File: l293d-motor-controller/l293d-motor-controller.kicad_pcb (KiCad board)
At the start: 2 copper layers, 49.6 x 66 mm, 19 parts, among them M1 Motor_DC, M2 Motor_DC, U1 LM7805, U2 L293D, U3 74HC04

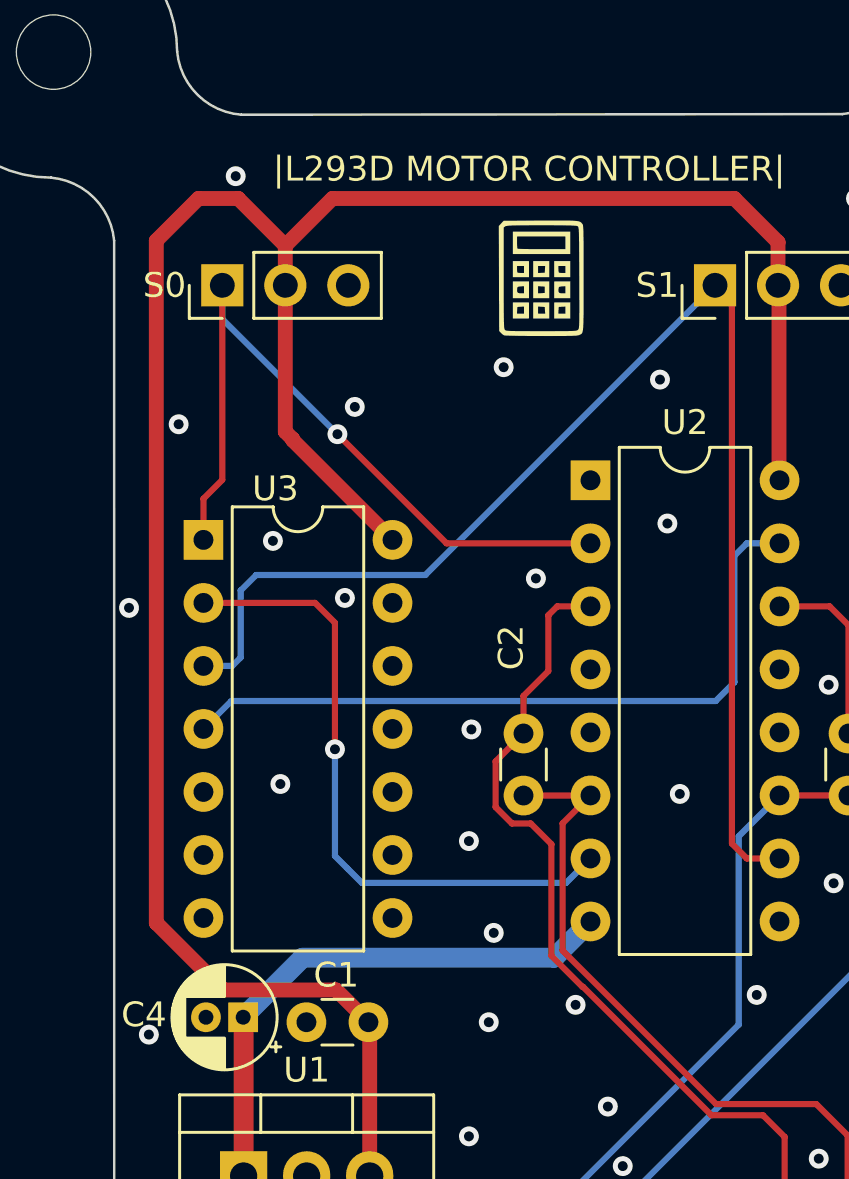
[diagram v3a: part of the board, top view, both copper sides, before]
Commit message: project 3 / l293d motor driver / 74hc04 changed to cd4069
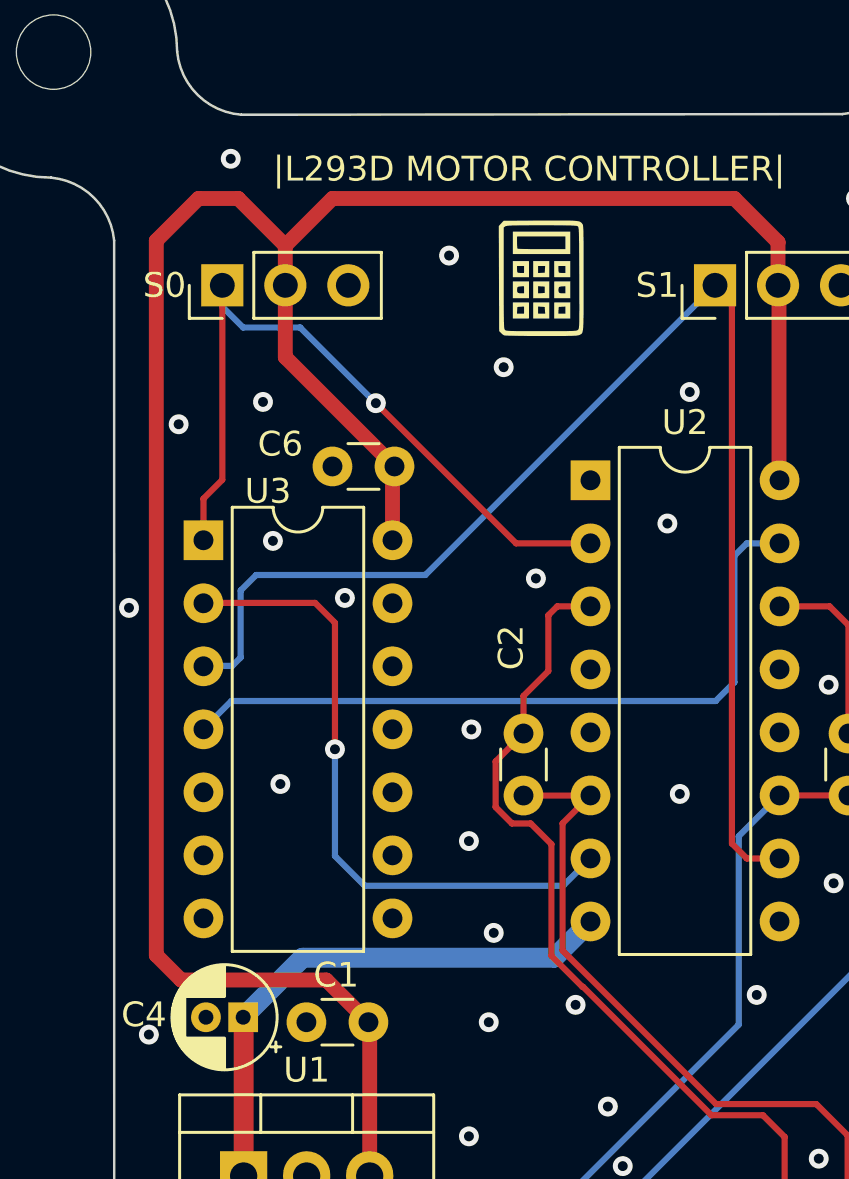
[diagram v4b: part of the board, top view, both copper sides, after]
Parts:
- added C6: 100n, Capacitor_THT:C_Disc_D3.0mm_W1.6mm_P2.50mm, F.Cu at (116.6, 110.7)
- U3: value 74HC04 -> 4069
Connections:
- U3 pad 11: unconnected-(U3-Q5-Pad11) -> GND
- U3 pad 13: unconnected-(U3-Q7-Pad13) -> GND
- U3 pad 5: unconnected-(U3-Q2-Pad5) -> GND
- U3 pad 9: unconnected-(U3-~{MR}-Pad9) -> GND
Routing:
- net +5V: track 96.0 -> 96.7 mm
- net GND: vias 35 -> 36

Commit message: project 3 / l293d motor controller / improved tracs
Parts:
- moved M1 10.3 mm to (121.8, 144.3)
- moved M2 8.38 mm to (132.2, 144.4)
- moved BT1 1.10 mm to (117.3, 144.3)
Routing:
- net Net-(M1--): track 30.7 -> 24.2 mm
- net Net-(M1-+): track 36.9 -> 31.0 mm
- net Net-(M2--): track 34.8 -> 31.6 mm
- net Net-(M2-+): track 26.7 -> 24.4 mm
- net +9V: track 36.1 -> 35.0 mm
- net GND: vias 36 -> 34

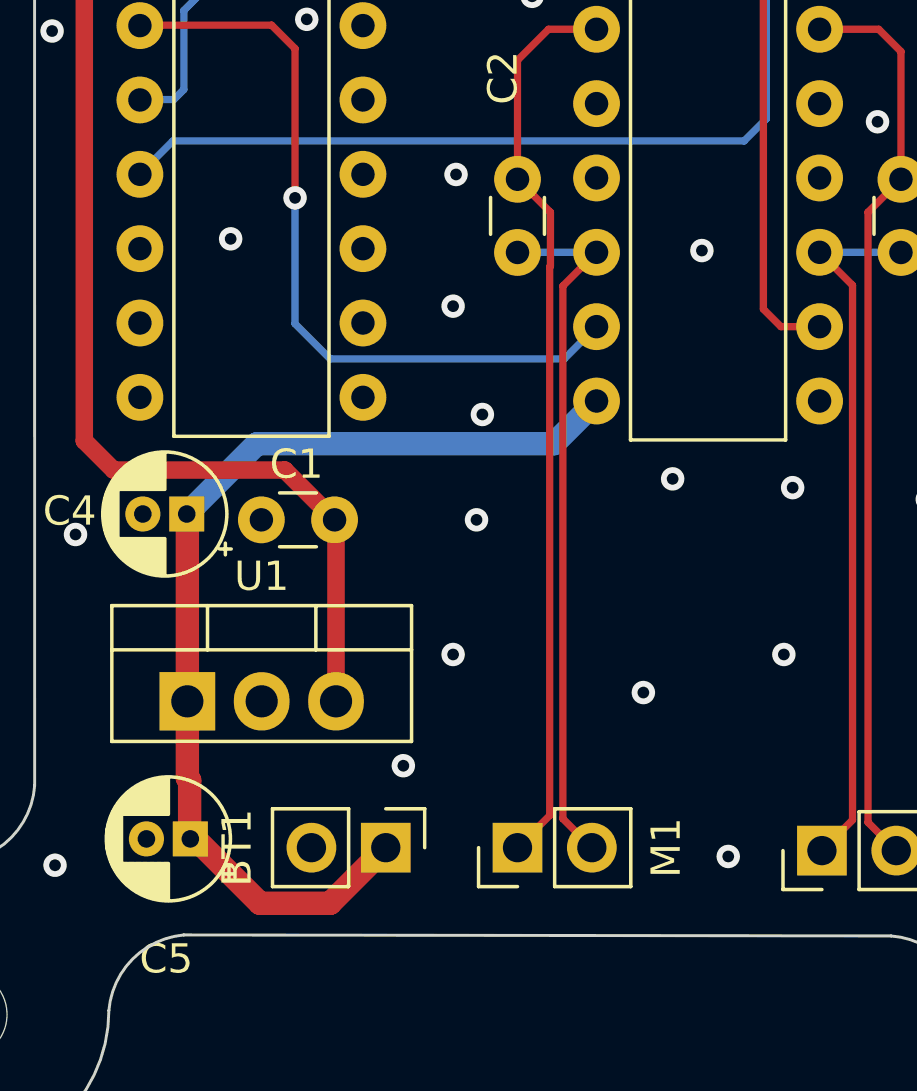
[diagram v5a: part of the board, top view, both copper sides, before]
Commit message: project 3 / l293d motor driver / VCC track changed
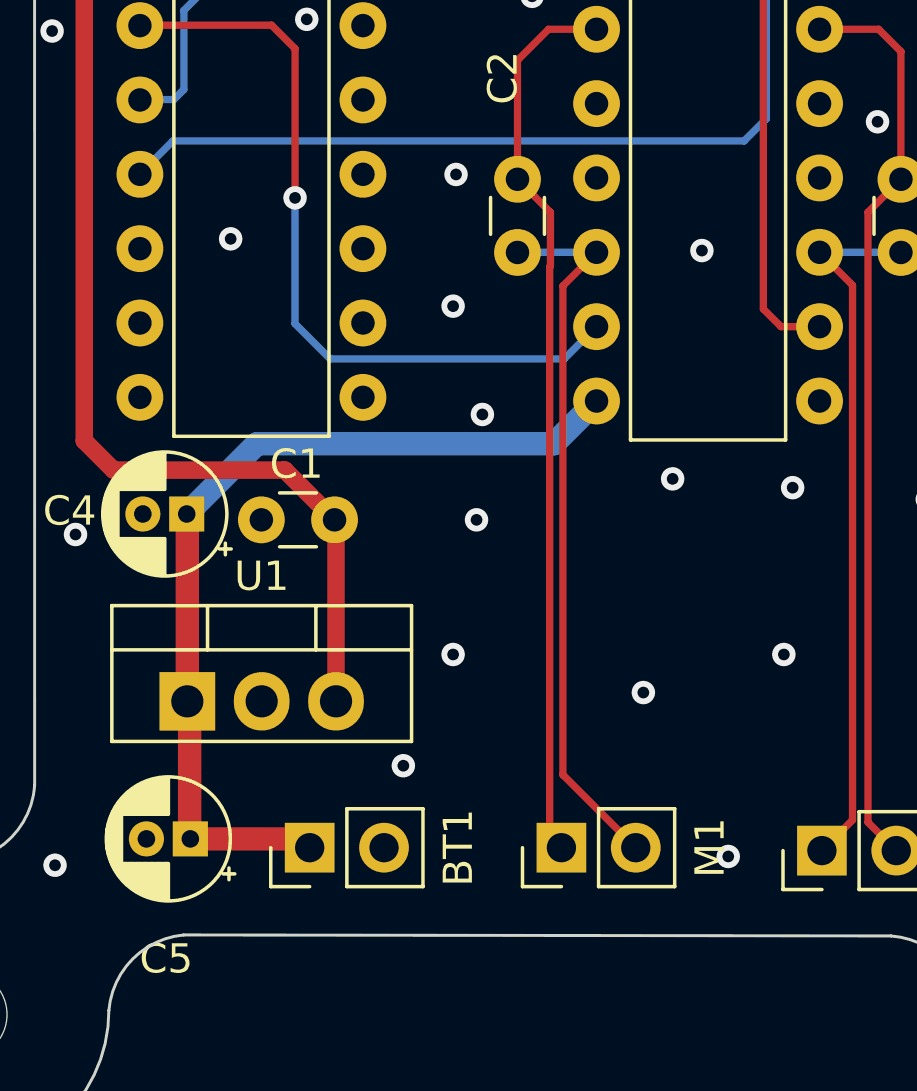
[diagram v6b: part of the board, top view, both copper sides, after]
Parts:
- moved BT1 2.60 mm to (114.7, 144.3), turned to 90 degrees
- moved M1 1.50 mm to (123.3, 144.3)
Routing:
- net +9V: track 35.0 -> 30.8 mm
- net Net-(M1--): track 24.2 -> 24.7 mm
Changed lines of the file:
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@@
   )
   (footprint "Connector_PinHeader_2.54mm:PinHeader_1x02_P2.54mm_Vertical" (layer "F.Cu")
-    (at 117.3 144.3 -90)
+    (at 114.7 144.3 90)
     (descr "Through hole straight pin header, 1x02, 2.54mm pitch, single row")
     (tags "Through hole pin header THT 1x02 2.54mm single row")
@@
     (fp_line (start 1.27 3.81) (end -1.27 3.81)
       (stroke (width 0.1) (type solid)) (layer "F.Fab"))
-    (pad "1" thru_hole rect (at 0 0 270) (size 1.7 1.7) (drill 1) (layers "*.Cu" "*.Mask")
+    (pad "1" thru_hole rect (at 0 0 90) (size 1.7 1.7) (drill 1) (layers "*.Cu" "*.Mask")
       (net 1 "+9V") (pinfunction "+") (pintype "passive"))
-    (pad "2" thru_hole oval (at 0 2.54 270) (size 1.7 1.7) (drill 1) (layers "*.Cu" "*.Mask")
+    (pad "2" thru_hole oval (at 0 2.54 90) (size 1.7 1.7) (drill 1) (layers "*.Cu" "*.Mask")
       (net 2 "GND") (pinfunction "-") (pintype "passive"))
     (model "${KICAD6_3DMODEL_DIR}/Connector_PinHeader_2.54mm.3dshapes/PinHeader_1x02_P2.54mm_Vertical.wrl"
@@
   )
   (footprint "Connector_PinHeader_2.54mm:PinHeader_1x02_P2.54mm_Vertical" (layer "F.Cu")
-    (at 121.8 144.3 90)
+    (at 123.3 144.3 90)
     (descr "Through hole straight pin header, 1x02, 2.54mm pitch, single row")
     (tags "Through hole pin header THT 1x02 2.54mm single row")
@@
     (effects (font (size 1 1) (thickness 0.15)) (justify left bottom))
   )
-  (segment (start 110.8 144) (end 113 146.2) (width 0.8) (layer "F.Cu") (net 1))
+  (segment (start 114.4 144) (end 114.7 144.3) (width 0.8) (layer "F.Cu") (net 1))
+  (segment (start 110.6226 144) (end 114.4 144) (width 0.8) (layer "F.Cu") (net 1))
   (segment (start 110.52 132.92) (end 110.5 132.9) (width 0.8) (layer "F.Cu") (net 1))
-  (segment (start 110.6 142) (end 110.52 141.92) (width 0.8) (layer "F.Cu") (net 1))
+  (segment (start 110.6 139.38) (end 110.52 139.3) (width 0.8) (layer "F.Cu") (net 1))
   (segment (start 110.52 139.3) (end 110.52 132.92) (width 0.8) (layer "F.Cu") (net 1))
-  (segment (start 115.4 146.2) (end 117.3 144.3) (width 0.8) (layer "F.Cu") (net 1))
-  (segment (start 113 146.2) (end 115.4 146.2) (width 0.8) (layer "F.Cu") (net 1))
-  (segment (start 110.6226 144) (end 110.8 144) (width 0.8) (layer "F.Cu") (net 1))
-  (segment (start 110.52 141.92) (end 110.52 139.3) (width 0.8) (layer "F.Cu") (net 1))
-  (segment (start 110.6 143.9) (end 110.6 142) (width 0.8) (layer "F.Cu") (net 1))
+  (segment (start 110.6 143.9) (end 110.6 139.38) (width 0.8) (layer "F.Cu") (net 1))
   (segment (start 110.5 132.9) (end 112.9 130.5) (width 0.8) (layer "B.Cu") (net 1))
   (segment (start 112.9 130.5) (end 123.04 130.5) (width 0.8) (layer "B.Cu") (net 1))
@@
   (via (at 108.3 109) (size 0.8) (drill 0.4) (layers "F.Cu" "B.Cu") (free) (net 2))
   (via (at 111.7 113.7) (size 0.8) (drill 0.4) (layers "F.Cu" "B.Cu") (free) (net 2))
-  (segment (start 122.9 143.2) (end 121.8 144.3) (width 0.25) (layer "F.Cu") (net 3))
+  (segment (start 122.9 143.9) (end 122.9 124.455991) (width 0.25) (layer "F.Cu") (net 3))
   (segment (start 121.8 117.4) (end 122.86 116.34) (width 0.25) (layer "F.Cu") (net 3))
   (segment (start 122.86 116.34) (end 124.5 116.34) (width 0.25) (layer "F.Cu") (net 3))
   (segment (start 121.8 121.465) (end 121.8 117.4) (width 0.25) (layer "F.Cu") (net 3))
-  (segment (start 122.925 124.430991) (end 122.9 124.455991) (width 0.25) (layer "F.Cu") (net 3))
-  (segment (start 122.9 124.455991) (end 122.9 143.2) (width 0.25) (layer "F.Cu") (net 3))
-  (segment (start 122.925 122.59) (end 122.925 124.430991) (width 0.25) (layer "F.Cu") (net 3))
-  (segment (start 121.8 121.465) (end 122.925 122.59) (width 0.25) (layer "F.Cu") (net 3))
+  (segment (start 123.3 144.3) (end 122.9 143.9) (width 0.25) (layer "F.Cu") (net 3))
+  (segment (start 122.9 124.455991) (end 122.925 124.430991) (width 0.25) (layer "F.Cu") (net 3))
+  (segment (start 122.925 122.59) (end 121.8 121.465) (width 0.25) (layer "F.Cu") (net 3))
+  (segment (start 122.925 124.430991) (end 122.925 122.59) (width 0.25) (layer "F.Cu") (net 3))
   (segment (start 132.12 123.96) (end 133.245 125.085) (width 0.25) (layer "F.Cu") (net 4))
   (segment (start 133.245 143.355) (end 132.2 144.4) (width 0.25) (layer "F.Cu") (net 4))
@@
   (segment (start 112.2 106.3) (end 112.2 103.4) (width 0.6) (layer "F.Cu") (net 10))
   (segment (start 108 131.4) (end 107 130.4) (width 0.6) (layer "F.Cu") (net 10))
-  (segment (start 123.35 125.11) (end 123.35 143.31) (width 0.25) (layer "F.Cu") (net 13))
-  (segment (start 123.35 143.31) (end 124.34 144.3) (width 0.25) (layer "F.Cu") (net 13))
+  (segment (start 123.35 141.81) (end 123.35 125.11) (width 0.25) (layer "F.Cu") (net 13))
+  (segment (start 125.84 144.3) (end 123.35 141.81) (width 0.25) (layer "F.Cu") (net 13))
   (segment (start 124.495 123.965) (end 124.5 123.96) (width 0.25) (layer "F.Cu") (net 13))
-  (segment (start 124.5 123.96) (end 123.35 125.11) (width 0.25) (layer "F.Cu") (net 13))
-  (segment (start 123.725 144.3) (end 123.825 144.3) (width 0.25) (layer "B.Cu") (net 13))
+  (segment (start 123.35 125.11) (end 124.5 123.96) (width 0.25) (layer "F.Cu") (net 13))
   (segment (start 121.735 123.965) (end 121.74 123.96) (width 0.25) (layer "B.Cu") (net 13))
   (segment (start 121.8 123.965) (end 121.735 123.965) (width 0.25) (layer "B.Cu") (net 13))
